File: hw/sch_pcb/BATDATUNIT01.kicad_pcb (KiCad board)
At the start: 2 copper layers, 136.2 x 85.9 mm, 223 parts, among them J1 USBC_USB4105-GF-A, J2 SD_Card-FPS009-4200-0, J3 HEADER_2x03, J4 46436-9327, Q1 BC817-25, Q2 BC817-25, Q3 BC817-25, Q4 BC817-25, Q5 BC817-25, Q6 BC817-25, Q7 BSS83P, SW1 SKRTLAE010, SW2 KMT031, SW3 SKRTLAE010, SW4 KMT031, U1 MAX14502AETL+, U10 PCF85263A, U11 TCA4307, U12 BQ34Z100, U13 BQ25628E, U14 SN74HC164P, U15 TPS631000DRLR, U16 TPS631000DRLR, U17 TPS631000DRLR, U18 TPS22965-Q1, U2 USBLC6-2SC6, U4 PCA9541ABS/01, U5 AT24CS64-SSHM, U6 SHT35-DIS, U7 TMUX1574DYYR, U8 ATMEGA1284P-AU, U9 MS561101BA03-50, Y1 19.2 MHz, Y2 8 MHz, Y3 ABS07-120-32.768KHZ-T

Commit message: Update components values to tested ones.
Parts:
- D3: value ORANGE -> GREEN
- D5: value ORANGE -> RED
- R22, R66, R67, R68, R69: value 180R -> 68R
- R26: value 270R -> 68R
- R3: value R -> 10k
- R4: value R -> 5k1
- R43: value 10M -> 1M
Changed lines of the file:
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@@
     (property "Sheetfile" "liion.kicad_sch")
     (property "Sheetname" "liion")
-    (property "UST_ID" "5c70984512875079b91f897c")
+    (property "UST_ID" "5c70984512875079b91f8975")
     (property "ki_description" "Resistor, small symbol")
     (property "ki_keywords" "R resistor")
@@
         (effects (font (size 0.8 0.8) (thickness 0.1)))
     )
-    (fp_text value "180R" (at 0 1.65) (layer "F.Fab")
+    (fp_text value "68R" (at 0 1.65) (layer "F.Fab")
         (effects (font (size 0.8 0.8) (thickness 0.1)))
     )
@@
     (property "Sheetfile" "liion.kicad_sch")
     (property "Sheetname" "liion")
-    (property "UST_ID" "5c70984512875079b91f897c")
+    (property "UST_ID" "5c70984512875079b91f8975")
     (property "ki_description" "Resistor, small symbol")
     (property "ki_keywords" "R resistor")
@@
         (effects (font (size 0.8 0.8) (thickness 0.1)))
     )
-    (fp_text value "180R" (at 0 1.65) (layer "F.Fab")
+    (fp_text value "68R" (at 0 1.65) (layer "F.Fab")
         (effects (font (size 0.8 0.8) (thickness 0.1)))
     )
@@
   (footprint "Mlab_D:SMD_LED_RIGHT_KINGBRIGHT_1605" (layer "F.Cu")
     (at 217.375 77.9 -90)
-    (property "LCSC" "C598394")
     (property "Sheetfile" "BATDATUNIT01.kicad_sch")
     (property "Sheetname" "")
@@
     (property "Sheetfile" "BATDATUNIT01.kicad_sch")
     (property "Sheetname" "")
-    (property "UST_ID" "5c70984512875079b91f897c")
+    (property "UST_ID" "5c70984512875079b91f8975")
     (property "ki_description" "Resistor, small symbol")
     (property "ki_keywords" "R resistor")
@@
         (effects (font (size 0.8 0.8) (thickness 0.1)))
     )
-    (fp_text value "180R" (at 0 1.65 90) (layer "F.Fab")
+    (fp_text value "68R" (at 0 1.65 90) (layer "F.Fab")
         (effects (font (size 0.8 0.8) (thickness 0.1)))
     )
@@
   (footprint "Mlab_D:SMD_LED_RIGHT_KINGBRIGHT_1605" (layer "F.Cu")
     (at 217.275 81.8 -90)
-    (property "LCSC" "C598398")
     (property "Sheetfile" "BATDATUNIT01.kicad_sch")
     (property "Sheetname" "")
@@
     (property "Sheetfile" "BATDATUNIT01.kicad_sch")
     (property "Sheetname" "")
-    (property "UST_ID" "65481fdd462c6d9e72056b6a")
+    (property "UST_ID" "65481f0c462c6d9e72056b3d")
     (property "ki_description" "Light emitting diode, small symbol")
     (property "ki_keywords" "LED diode light-emitting-diode")
@@
         (effects (font (size 0.8 0.8) (thickness 0.1)))
     )
-    (fp_text value "ORANGE" (at 0 1 -90 unlocked) (layer "F.Fab") hide
+    (fp_text value "GREEN" (at 0 1 -90 unlocked) (layer "F.Fab") hide
         (effects (font (size 0.8 0.8) (thickness 0.1)))
     )
@@
     (property "Sheetfile" "liion.kicad_sch")
     (property "Sheetname" "liion")
-    (property "UST_ID" "5c70984512875079b91f897c")
+    (property "UST_ID" "5c70984512875079b91f8975")
     (property "ki_description" "Resistor, small symbol")
     (property "ki_keywords" "R resistor")
@@
         (effects (font (size 0.8 0.8) (thickness 0.1)))
     )
-    (fp_text value "180R" (at 0 1.65) (layer "F.Fab")
+    (fp_text value "68R" (at 0 1.65) (layer "F.Fab")
         (effects (font (size 0.8 0.8) (thickness 0.1)))
     )
@@
     (property "Sheetfile" "BATDATUNIT01.kicad_sch")
     (property "Sheetname" "")
-    (property "UST_ID" "65481fdd462c6d9e72056b6a")
+    (property "UST_ID" "65481f96462c6d9e72056b54")
     (property "ki_description" "Light emitting diode, small symbol")
     (property "ki_keywords" "LED diode light-emitting-diode")
@@
         (effects (font (size 0.8 0.8) (thickness 0.1)))
     )
-    (fp_text value "ORANGE" (at 0 1 -90 unlocked) (layer "F.Fab") hide
+    (fp_text value "RED" (at 0 1 -90 unlocked) (layer "F.Fab") hide
         (effects (font (size 0.8 0.8) (thickness 0.1)))
     )
@@
     (property "Sheetfile" "liion.kicad_sch")
     (property "Sheetname" "liion")
-    (property "UST_ID" "5c70984512875079b91f897c")
+    (property "UST_ID" "5c70984512875079b91f8975")
     (property "ki_description" "Resistor, small symbol")
     (property "ki_keywords" "R resistor")
@@
         (effects (font (size 0.8 0.8) (thickness 0.1)))
     )
-    (fp_text value "180R" (at 0 1.65) (layer "F.Fab")
+    (fp_text value "68R" (at 0 1.65) (layer "F.Fab")
         (effects (font (size 0.8 0.8) (thickness 0.1)))
     )
@@
     (property "Sheetfile" "BATDATUNIT01.kicad_sch")
     (property "Sheetname" "")
-    (property "UST_ID" "5c70984712875079b91f8aae")
+    (property "UST_ID" "5c70984712875079b91f8aaa")
     (property "ki_description" "Resistor, small symbol")
     (property "ki_keywords" "R resistor")
@@
         (effects (font (size 0.8 0.8) (thickness 0.1)) (justify mirror))
     )
-    (fp_text value "10M" (at 0 -1.65) (layer "B.Fab")
+    (fp_text value "1M" (at 0 -1.65) (layer "B.Fab")
         (effects (font (size 1 1) (thickness 0.15)) (justify mirror))
     )
@@
     (descr "Resistor SMD 0805 (2012 Metric), square (rectangular) end terminal, IPC_7351 nominal, (Body size source: IPC-SM-782 page 72, https://www.pcb-3d.com/wordpress/wp-content/uploads/ipc-sm-782a_amendment_1_and_2.pdf), generated with kicad-footprint-generator")
     (tags "resistor")
-    (property "Pole4" "")
     (property "Sheetfile" "BATDATUNIT01.kicad_sch")
     (property "Sheetname" "")
-    (property "UST_ID" "5c70984512875079b91f8983")
+    (property "UST_ID" "5c70984512875079b91f8975")
     (property "ki_description" "Resistor, small symbol")
     (property "ki_keywords" "R resistor")
@@
         (effects (font (size 0.8 0.8) (thickness 0.1)) (justify mirror))
     )
-    (fp_text value "270R" (at 0 -1.65 90) (layer "B.Fab")
+    (fp_text value "68R" (at 0 -1.65 90) (layer "B.Fab")
         (effects (font (size 0.8 0.8) (thickness 0.1)) (justify mirror))
     )
@@
         (effects (font (size 0.8 0.8) (thickness 0.1)) (justify mirror))
     )
-    (fp_text value "R" (at 0 -1.65 90) (layer "B.Fab")
+    (fp_text value "5k1" (at 0 -1.65 90) (layer "B.Fab")
         (effects (font (size 1 1) (thickness 0.15)) (justify mirror))
     )
@@
         (effects (font (size 0.8 0.8) (thickness 0.1)) (justify mirror))
     )
-    (fp_text value "R" (at 0 -1.65 -270) (layer "B.Fab")
+    (fp_text value "10k" (at 0 -1.65 -270) (layer "B.Fab")
         (effects (font (size 1 1) (thickness 0.15)) (justify mirror))
     )

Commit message: Update and correct values from manufacturing process.
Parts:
- Q5, Q6: value BC817-25 -> BC807-25
- R51: value 270R -> 68R
- U6: value SHT35-DIS -> SHT31-DIS
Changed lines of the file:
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@@
     (property "Sheetfile" "BATDATUNIT01.kicad_sch")
     (property "Sheetname" "")
-    (property "UST_ID" "")
+    (property "UST_ID" "5c70984612875079b91f899f")
     (property "ki_description" "Resistor, small symbol")
     (property "ki_keywords" "R resistor")
@@
     (property "Sheetfile" "BATDATUNIT01.kicad_sch")
     (property "Sheetname" "")
+    (property "UST_ID" "5c70984712875079b91f8b53")
     (property "ki_description" "Unpolarized capacitor, small symbol")
     (property "ki_keywords" "capacitor cap")
@@
         (effects (font (size 0.8 0.8) (thickness 0.1)) (justify mirror))
     )
-    (fp_text value "BC817-25" (at 0 -2.4 -270) (layer "B.Fab")
+    (fp_text value "BC807-25" (at 0 -2.4 -270) (layer "B.Fab")
         (effects (font (size 0.8 0.8) (thickness 0.1)) (justify mirror))
     )
@@
     (property "Sheetfile" "sw_source.kicad_sch")
     (property "Sheetname" "sw_source")
-    (property "UST_ID" "")
+    (property "UST_ID" "5c70984612875079b91f899f")
     (property "ki_description" "Resistor, small symbol")
     (property "ki_keywords" "R resistor")
@@
     (property "Sheetfile" "liion.kicad_sch")
     (property "Sheetname" "liion")
-    (property "UST_ID" "5c70984512875079b91f8983")
+    (property "UST_ID" "5c70984512875079b91f8975")
     (property "ki_description" "Resistor, small symbol")
     (property "ki_keywords" "R resistor")
@@
         (effects (font (size 0.8 0.8) (thickness 0.1)) (justify mirror))
     )
-    (fp_text value "270R" (at 0 -1.65 90) (layer "B.Fab")
+    (fp_text value "68R" (at 0 -1.65 90) (layer "B.Fab")
         (effects (font (size 0.8 0.8) (thickness 0.1)) (justify mirror))
     )
@@
         (effects (font (size 0.8 0.8) (thickness 0.1)) (justify mirror))
     )
-    (fp_text value "BC817-25" (at 0 -2.4 90) (layer "B.Fab")
+    (fp_text value "BC807-25" (at 0 -2.4 90) (layer "B.Fab")
         (effects (font (size 0.8 0.8) (thickness 0.1)) (justify mirror))
     )
@@
     (property "Sheetfile" "BATDATUNIT01.kicad_sch")
     (property "Sheetname" "")
-    (property "UST_ID" "")
+    (property "UST_ID" "5c70984612875079b91f899f")
     (property "ki_description" "Resistor, small symbol")
     (property "ki_keywords" "R resistor")
@@
     (property "Sheetfile" "BATDATUNIT01.kicad_sch")
     (property "Sheetname" "")
-    (property "UST_ID" "")
+    (property "UST_ID" "5c70984612875079b91f899f")
     (property "ki_description" "Resistor, small symbol")
     (property "ki_keywords" "R resistor")
@@
     (property "Sheetfile" "BATDATUNIT01.kicad_sch")
     (property "Sheetname" "")
-    (property "UST_ID" "")
+    (property "UST_ID" "5c70984612875079b91f899f")
     (property "ki_description" "Resistor, small symbol")
     (property "ki_keywords" "R resistor")
@@
     (property "Sheetfile" "BATDATUNIT01.kicad_sch")
     (property "Sheetname" "")
-    (property "UST_ID" "65103c42462c6d9e72054b8e")
+    (property "UST_ID" "5c70984612875079b91f89e4")
     (property "ki_description" "I²C humidity and temperature sensor, ±1.5%RH, ±0.1°C, DFN-8")
     (property "ki_keywords" "digital temperature humidity i2c")
@@
         (effects (font (size 0.8 0.8) (thickness 0.1)) (justify mirror))
     )
-    (fp_text value "SHT35-DIS" (at 0 -2.5 90) (layer "B.Fab")
+    (fp_text value "SHT31-DIS" (at 0 -2.5 90) (layer "B.Fab")
         (effects (font (size 0.8 0.8) (thickness 0.1)) (justify mirror))
     )
@@
     (property "Sheetfile" "BATDATUNIT01.kicad_sch")
     (property "Sheetname" "")
+    (property "UST_ID" "5c70984612875079b91f899f")
     (property "ki_description" "Resistor, small symbol")
     (property "ki_keywords" "R resistor")
@@
     (property "Sheetfile" "sw_source.kicad_sch")
     (property "Sheetname" "sw_source")
-    (property "UST_ID" "")
+    (property "UST_ID" "5c70984612875079b91f899f")
     (property "ki_description" "Resistor, small symbol")
     (property "ki_keywords" "R resistor")
@@
     (property "Sheetfile" "BATDATUNIT01.kicad_sch")
     (property "Sheetname" "")
-    (property "UST_ID" "")
+    (property "UST_ID" "5c70984612875079b91f899f")
     (property "ki_description" "Resistor, small symbol")
     (property "ki_keywords" "R resistor")
@@
     (property "Sheetfile" "BATDATUNIT01.kicad_sch")
     (property "Sheetname" "")
-    (property "UST_ID" "")
+    (property "UST_ID" "5c70984612875079b91f899f")
     (property "ki_description" "Resistor, small symbol")
     (property "ki_keywords" "R resistor")
@@
     (property "Sheetfile" "BATDATUNIT01.kicad_sch")
     (property "Sheetname" "")
-    (property "UST_ID" "")
+    (property "UST_ID" "5c70984612875079b91f899f")
     (property "ki_description" "Resistor, small symbol")
     (property "ki_keywords" "R resistor")
@@
     (property "Sheetfile" "BATDATUNIT01.kicad_sch")
     (property "Sheetname" "")
-    (property "UST_ID" "")
+    (property "UST_ID" "5c70984612875079b91f899f")
     (property "ki_description" "Resistor, small symbol")
     (property "ki_keywords" "R resistor")

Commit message: Update the commponent values according to actual component values used during manufacturing.
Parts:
- R14: value 27k -> 25k5
- R56: value 2k49 -> 2k4
- R57: value 5k3 -> 5k1
- R58: value 31k1 -> 33k
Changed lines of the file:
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@@
     (property "Sheetfile" "BATDATUNIT01.kicad_sch")
     (property "Sheetname" "")
-    (property "UST_ID" "")
+    (property "UST_ID" "5c70984712875079b91f8a88")
     (property "ki_description" "Resistor, small symbol")
     (property "ki_keywords" "R resistor")
@@
         (effects (font (size 0.8 0.8) (thickness 0.1)) (justify mirror))
     )
-    (fp_text value "27k" (at 0 -1.65 90) (layer "B.Fab")
+    (fp_text value "25k5" (at 0 -1.65 90) (layer "B.Fab")
         (effects (font (size 0.8 0.8) (thickness 0.1)) (justify mirror))
     )
@@
         (effects (font (size 0.8 0.8) (thickness 0.1)) (justify mirror))
     )
-    (fp_text value "2k49" (at 0 -1.65 90) (layer "B.Fab")
+    (fp_text value "2k4" (at 0 -1.65 90) (layer "B.Fab")
         (effects (font (size 0.8 0.8) (thickness 0.1)) (justify mirror))
     )
@@
         (effects (font (size 0.8 0.8) (thickness 0.1)) (justify mirror))
     )
-    (fp_text value "5k3" (at 0 -1.65 90) (layer "B.Fab")
+    (fp_text value "5k1" (at 0 -1.65 90) (layer "B.Fab")
         (effects (font (size 0.8 0.8) (thickness 0.1)) (justify mirror))
     )
@@
         (effects (font (size 0.8 0.8) (thickness 0.1)) (justify mirror))
     )
-    (fp_text value "31k1" (at 0 -1.65 90) (layer "B.Fab")
+    (fp_text value "33k" (at 0 -1.65 90) (layer "B.Fab")
         (effects (font (size 0.8 0.8) (thickness 0.1)) (justify mirror))
     )

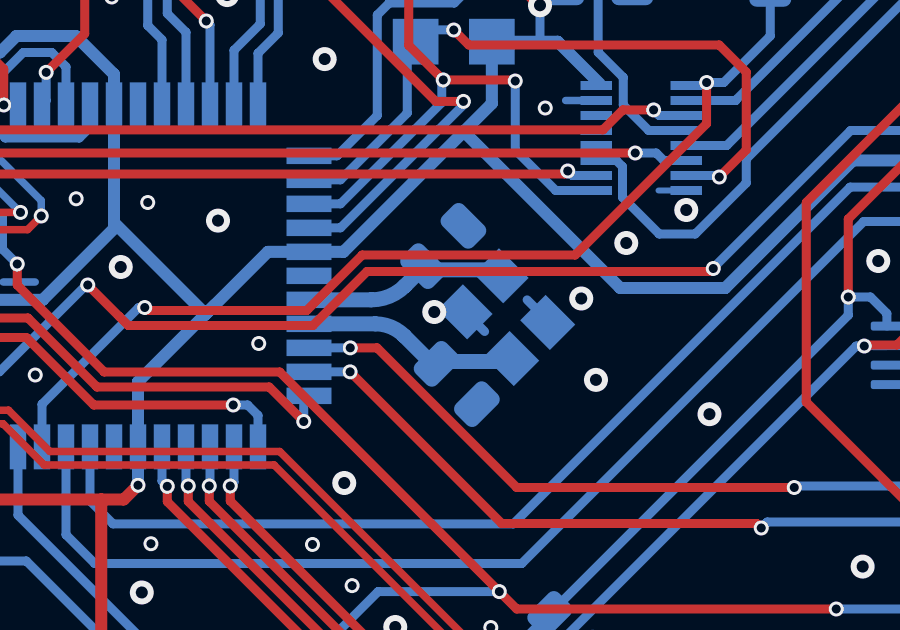
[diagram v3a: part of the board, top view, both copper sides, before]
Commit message: Silkscreen improvement.
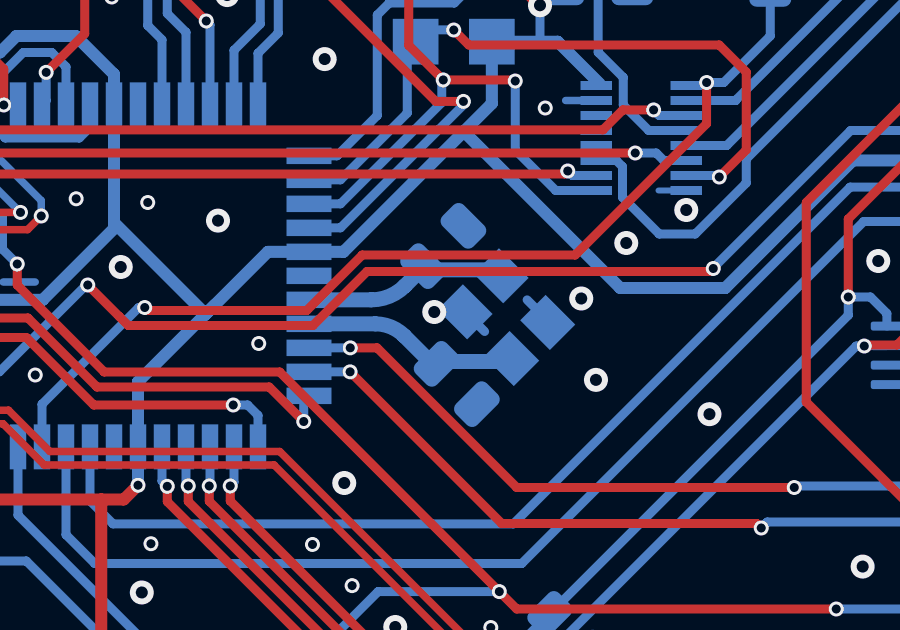
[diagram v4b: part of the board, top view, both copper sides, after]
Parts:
- renumbered locked to U3

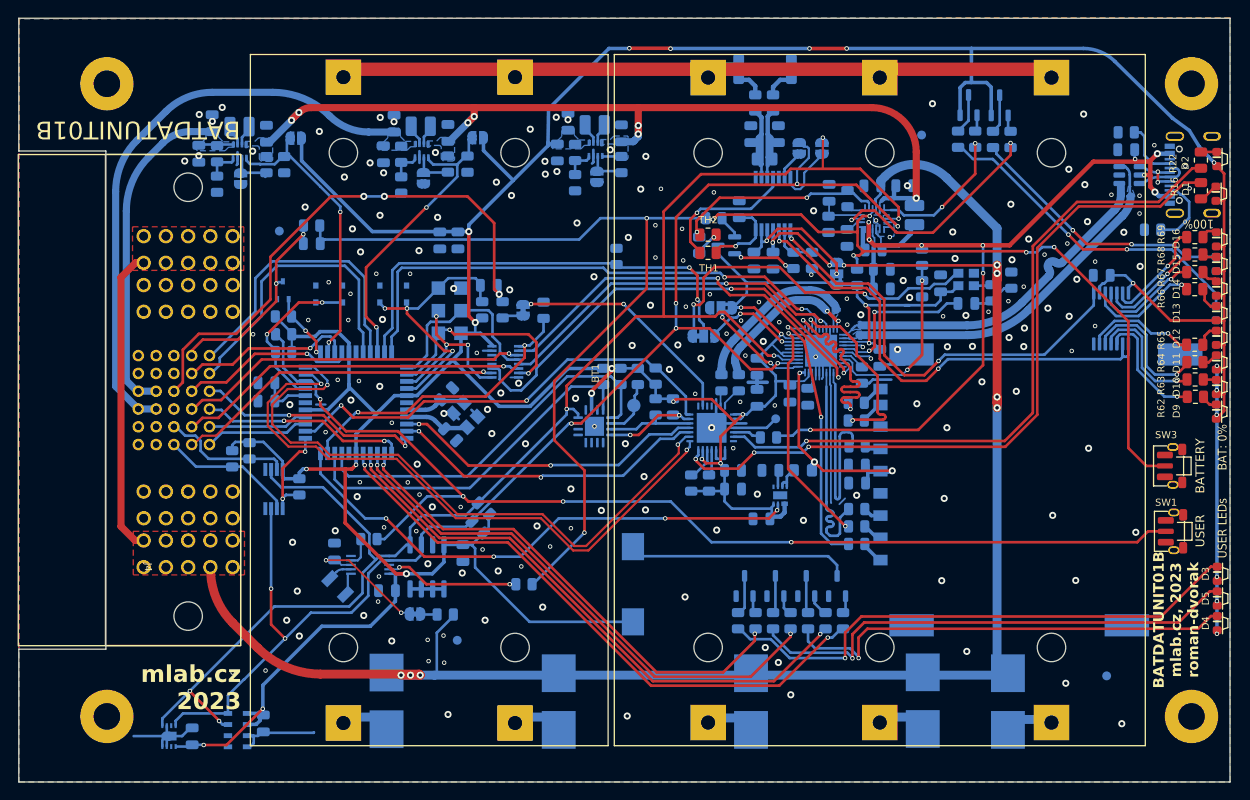
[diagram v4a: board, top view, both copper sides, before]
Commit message: Convert to KiCAD 9 Add CR2032 battery holder to avoid RTC reset with removed accumulators.
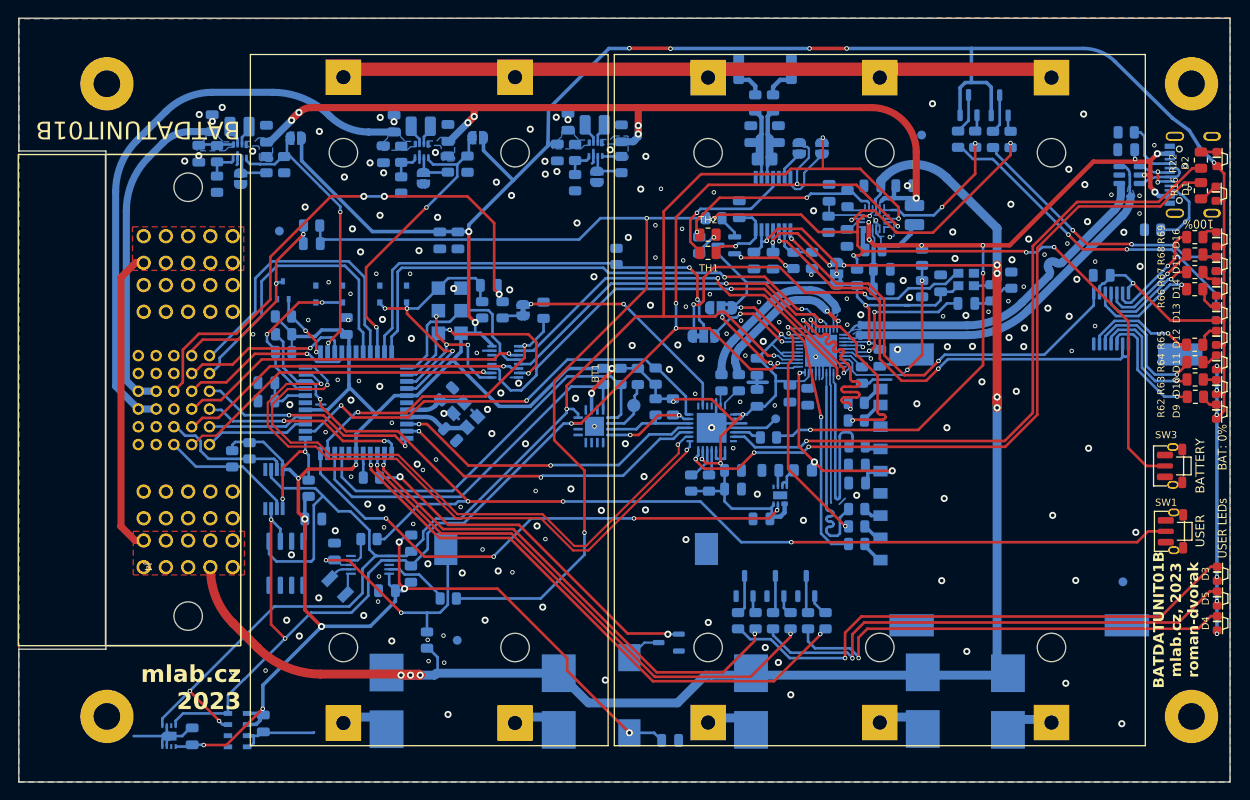
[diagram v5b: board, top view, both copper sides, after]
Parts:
- removed JP4: SolderJumper_2_Open, Jumper:SolderJumper-2_P1.3mm_Bridged_RoundedPad1.0x1.5mm
- added BT3: CR2032, Battery:BatteryHolder_Keystone_1060_1x2032, B.Cu at (145.4, 121.7)
- added C51: 100n, Capacitor_SMD:C_0805_2012Metric, B.Cu at (119.5, 96.7)
- added C52: 100n, Capacitor_SMD:C_0805_2012Metric, B.Cu at (155.9, 143.3)
- C21: value 10u -> 22u
- R43: value 1M -> 270k
- moved R32 55.4 mm to (122.4, 113.7), turned to 0 degrees
- moved Q4 20.0 mm to (155.8, 132.3), turned to 180 degrees
- moved C50 17.2 mm to (115.8, 118.4), turned to 0 degrees
- moved U5 15.9 mm to (112.8, 123.3)
- moved BZ1 12.5 mm to (151.3, 138.2)
- moved FID4 10.7 mm to (206.8, 125.4)
- moved R37 9.16 mm to (126.8, 124.6), turned to -90 degrees
- moved R36 9.05 mm to (126.8, 121.1), turned to 90 degrees
- moved R45 8.66 mm to (131.0, 127.3)
- moved R41 3.53 mm to (128.6, 132.0), turned to -90 degrees
- moved R42 1.05 mm to (115.3, 114.9), turned to -90 degrees
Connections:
- C20 pad 1: Net-(JP4-B) -> Net-(BT3-+)
- R41 pad 1: Net-(JP4-A) -> Net-(BT3-+)
- U10 pad 3: Net-(JP4-B) -> Net-(BT3-+)
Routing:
- net /buzzer: track 68.1 -> 2.73 mm, vias 2 -> 0
- net Net-(Q4-B): track 1.97 -> 41.0 mm, vias 0 -> 2
- net Net-(BT3-+): track 0.00 -> 28.1 mm, vias 0 -> 2
- net Net-(BZ1-+): track 23.5 -> 3.99 mm
- net Net-(JP4-B): track 14.9 -> 0.00 mm, vias 2 -> 0
- net SDA_I2C: track 171.8 -> 185.8 mm
- net +3.3V: track 569.4 -> 583.2 mm, vias 29 -> 33
- net EXT_DETECTION_CHARGER: track 176.1 -> 186.7 mm
- net Net-(U10-INTA): track 15.1 -> 7.28 mm, vias 2 -> 0
- net GND: track 82.5 -> 78.4 mm
- net SCL_I2C: track 158.9 -> 162.0 mm
- net /SCL_MCU: track 43.1 -> 44.9 mm
- net Net-(JP4-A): track 1.86 -> 0.00 mm
- net unconnected-(U1-~{BUSY}-Pad7): track 1.60 -> 0.00 mm
- net unconnected-(U1-~{BERR}/INT-Pad6): track 1.55 -> 0.00 mm
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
